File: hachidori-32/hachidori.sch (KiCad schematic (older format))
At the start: 55 parts, among them P1 VIN, P2 UART, P3 ADC, P4 I2C, SW1 FLASH, SW2 RESET, U1 NCP1117ST33, U2 MPU-9250, U3 ESP-13-WROOM-02, U4 BME280, U7 INA226

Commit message: Change esp chip
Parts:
- removed LED4, LED5: Front, droneworks:LED_1608mm, symbol LED-RESCUE-hachidori
- removed LED6, LED7: Back, droneworks:LED_1608mm, symbol LED-RESCUE-hachidori
- removed R28, R29, R30, R31: 220, rohm:MCR03, symbol R
- removed R3: 10k, rohm:MCR03, symbol R
- removed U3: ESP-13-WROOM-02, droneworks:ESP-WROOM-02, symbol ESP-13-WROOM-02
- removed U?: 74AUP1G19, symbol 74AUP1G19
- added U?: ESP-WROOM-32, symbol ESP-WROOM-32
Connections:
- net labels removed: CS_2MP
- wire segments 291 -> 171
- no-connect marks 6 -> 5
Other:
- moved on the sheet: CB10, CB11, CB5, CB6, P2, P3, P4, R10, R26, R27, R4, R5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

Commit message: fix connections
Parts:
- removed CB? (x3): 104, droneworks:GRM18, symbol C
- removed P3: ADC, droneworks:Pin_Header_1x03, symbol CONN_01X03
- removed P?: SWD, symbol CONN_01X04
- removed P? (x2): PIO, symbol CONN_01X04
- removed P?: PIO, droneworks:Pin_Header_1x03, symbol CONN_01X03
- removed R2, R5: 10k, rohm:MCR03, symbol R
- removed R6: 20k, rohm:MCR03, symbol R
- removed R8: 2k, rohm:MCR03, symbol R
- removed U?: LPC812M101JDH20, symbol LPC812M101JDH20
- added P?: PWM, droneworks:Pin_Header_1x04, symbol CONN_01X04
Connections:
- net labels added: CS1, U2RXD, U2TXD, VBUS, VIN+, VIN-, VSPI_CLK, VSPI_CS0, VSPI_MISO, VSPI_MOSI
- net labels removed: ESP-RXD, ESP-TXD, HSPI_CLK, HSPI_CS, HSPI_MISO, HSPI_MOSI, LPC_CS, MPU_CS, SWCLK, SWDIO, TOUT, TOUTpin
- wire segments 171 -> 179
- no-connect marks 5 -> 11
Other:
- note added: "MPU_SPI0_CS"
- note added: "MPU_SPI0_SCLK"
- note removed: "I2C_SCL"
- note removed: "I2C_SDA"
- note removed: "LPC_SPI0_SI"
- note removed: "LPC_SPI0_SLK"
- note removed: "LPC_SPI0_SO"
- note removed: "MPU_SPI0_SLK"
- moved on the sheet: CB1, CB10, CB11, CB2, CB3, CB4, CB5, CB6, CE1, CE2, LED1, P1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

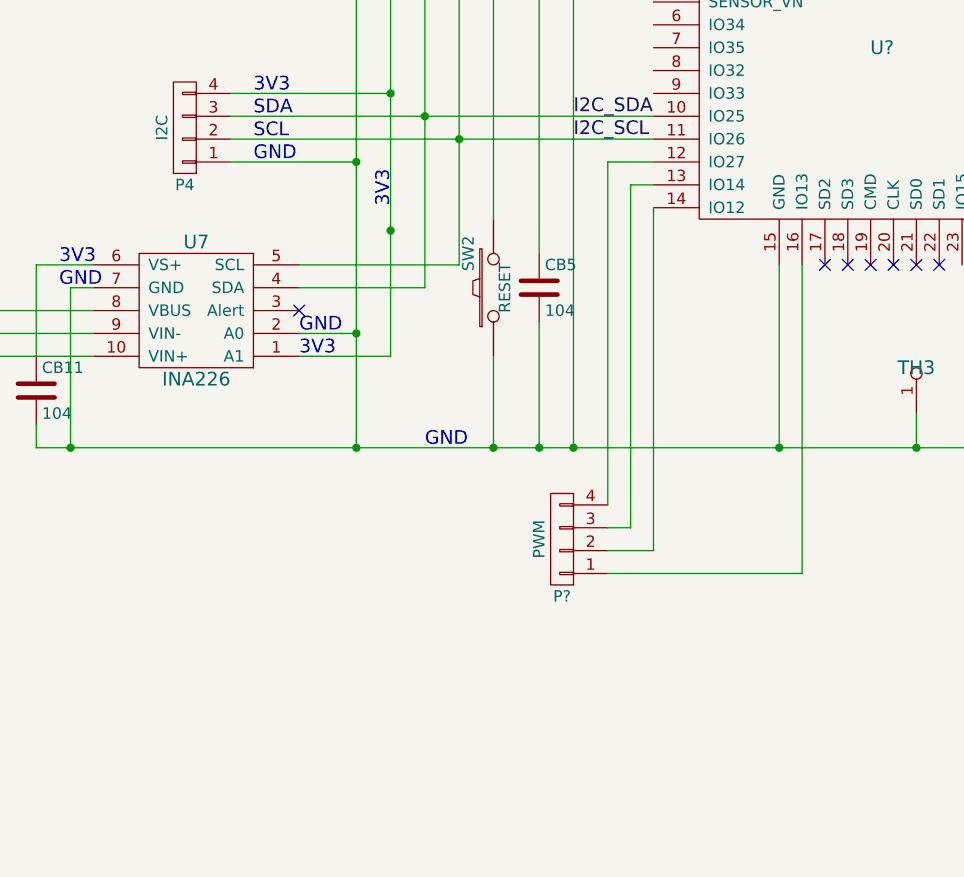
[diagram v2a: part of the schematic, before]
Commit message: Add ESC Interface
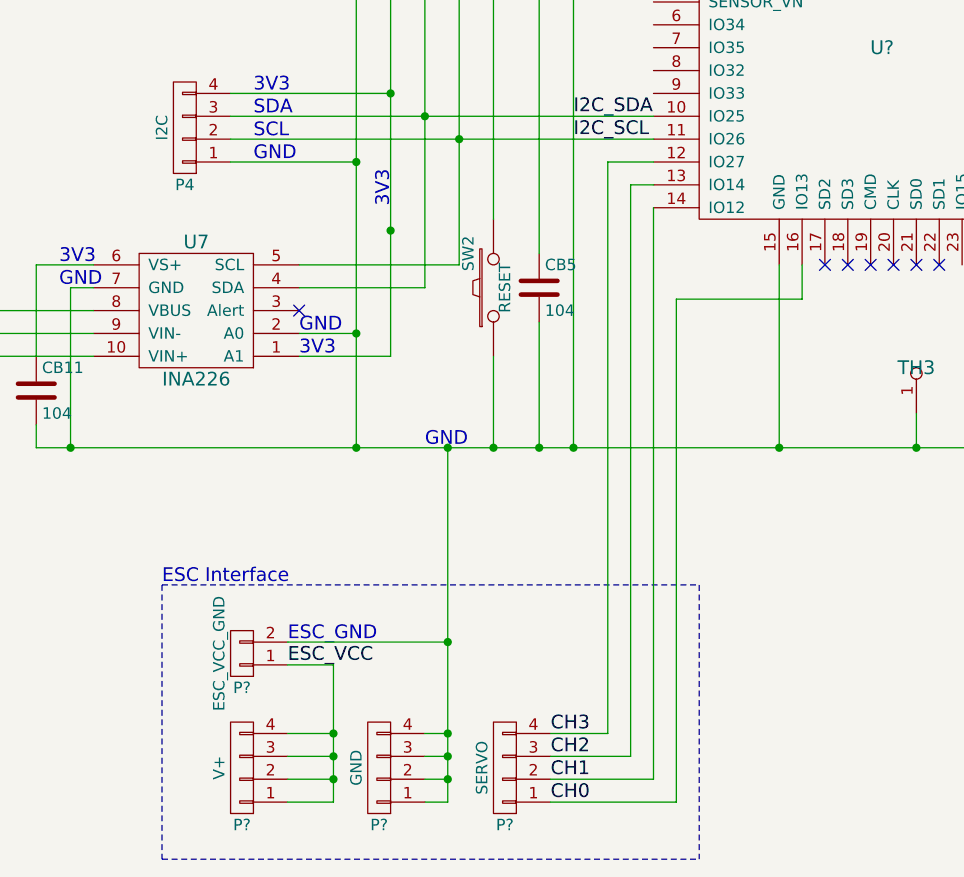
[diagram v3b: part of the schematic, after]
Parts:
- added P?: GND, droneworks:Pin_Header_1x04, symbol CONN_01X04
- added P?: V+, droneworks:Pin_Header_1x04, symbol CONN_01X04
- added P?: ESC_VCC_GND, droneworks:Pin_Header_1x02, symbol CONN_01X02
- P?: value PWM -> SERVO
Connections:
- net GND: now also P?.1 (P1), P?.2 (P2), P?.2 (P2), P?.3 (P3), P?.4 (P4)
- net CH3: now reaches P?.4 (P4), U?.12 (IO27)
- net CH2: now reaches P?.3 (P3), U?.13 (IO14)
- net CH1: now reaches P?.2 (P2), U?.14 (IO12)
- net CH0: now reaches P?.1 (P1), U?.16 (IO13)
- new net ESC_VCC: P?.1 (P1), P?.1 (P1), P?.2 (P2), P?.3 (P3), P?.4 (P4)
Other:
- note added: "ESC Interface"
- note added: "ESC_GND"
- moved on the sheet: P?

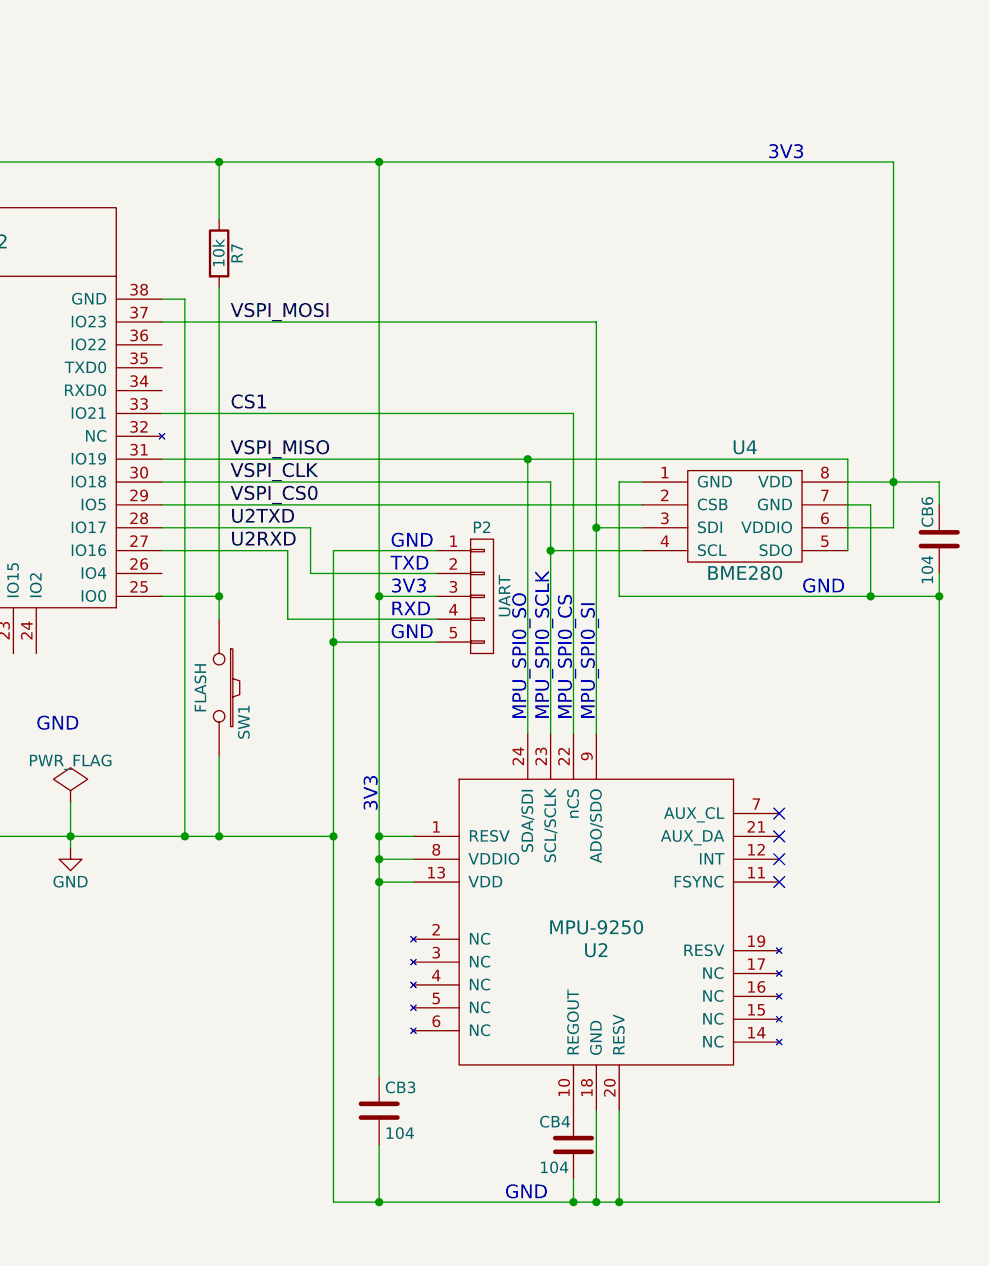
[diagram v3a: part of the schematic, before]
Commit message: Add UART Interface
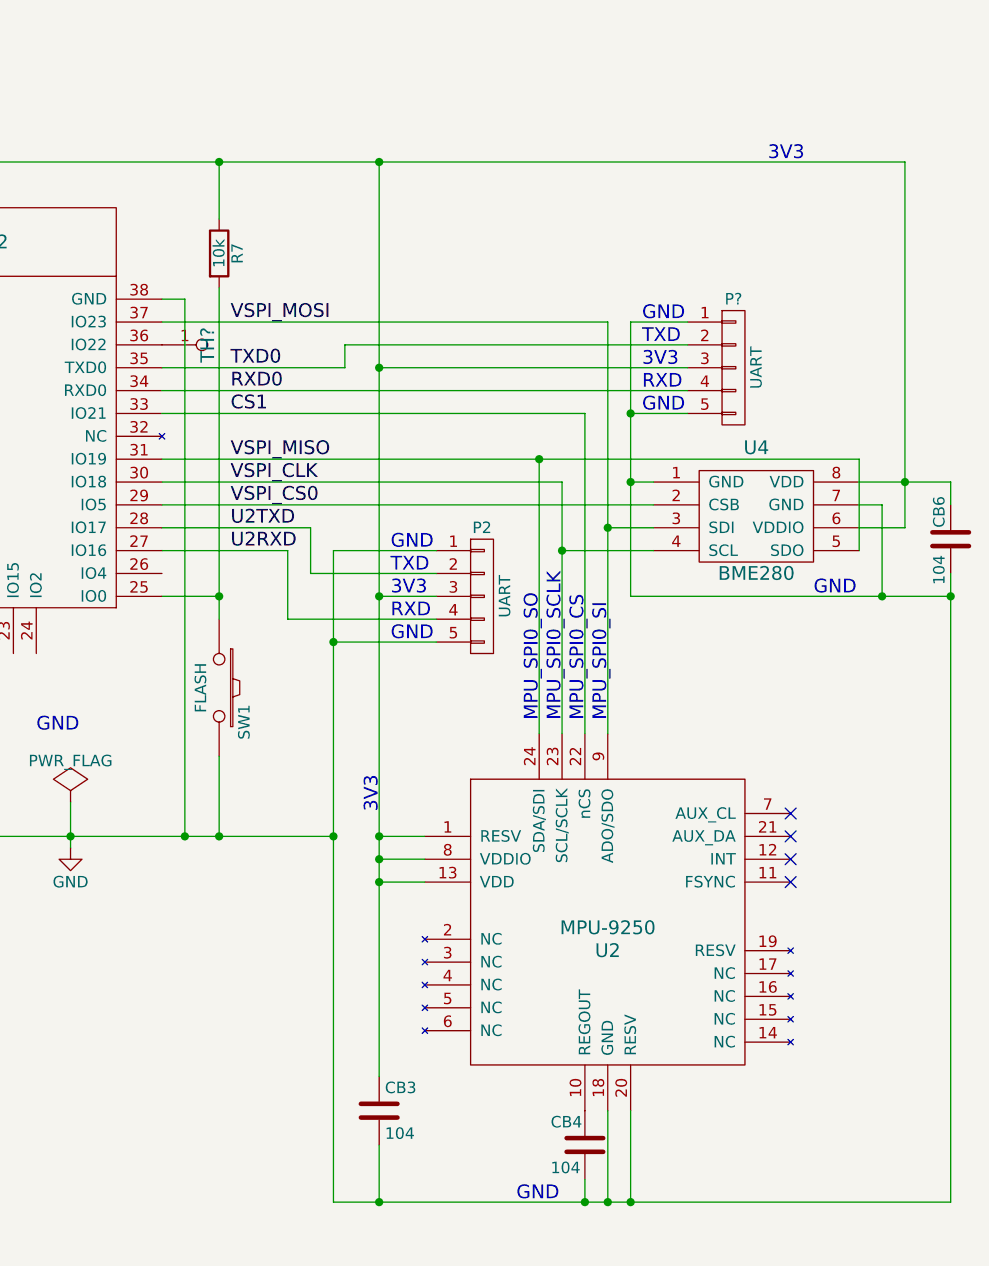
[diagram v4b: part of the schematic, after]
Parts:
- added P?: UART, droneworks:Pin_Header_1x05, symbol CONN_01X05
- added TH?: GND, droneworks:TH, symbol throughhole
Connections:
- net 3V3: now also P?.3 (P3)
- net GND: now also P?.1 (P1), P?.5 (P5)
- net RXD0: now reaches U?.34 (RXD0)
- net RXD0: now also P?.4 (P4)
- net TXD0: now reaches U?.35 (TXD0)
- net TXD0: now also P?.2 (P2)
- net at U?.36 (IO22): now also TH?.1
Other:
- moved on the sheet: CB4, CB6, U2, U4

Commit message: fix wire
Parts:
- P?: value UART -> Program
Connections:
- net FLASH: now reaches R7.2, SW1.1, U?.25 (IO0)
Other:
- moved on the sheet: P?, SW1, TH3

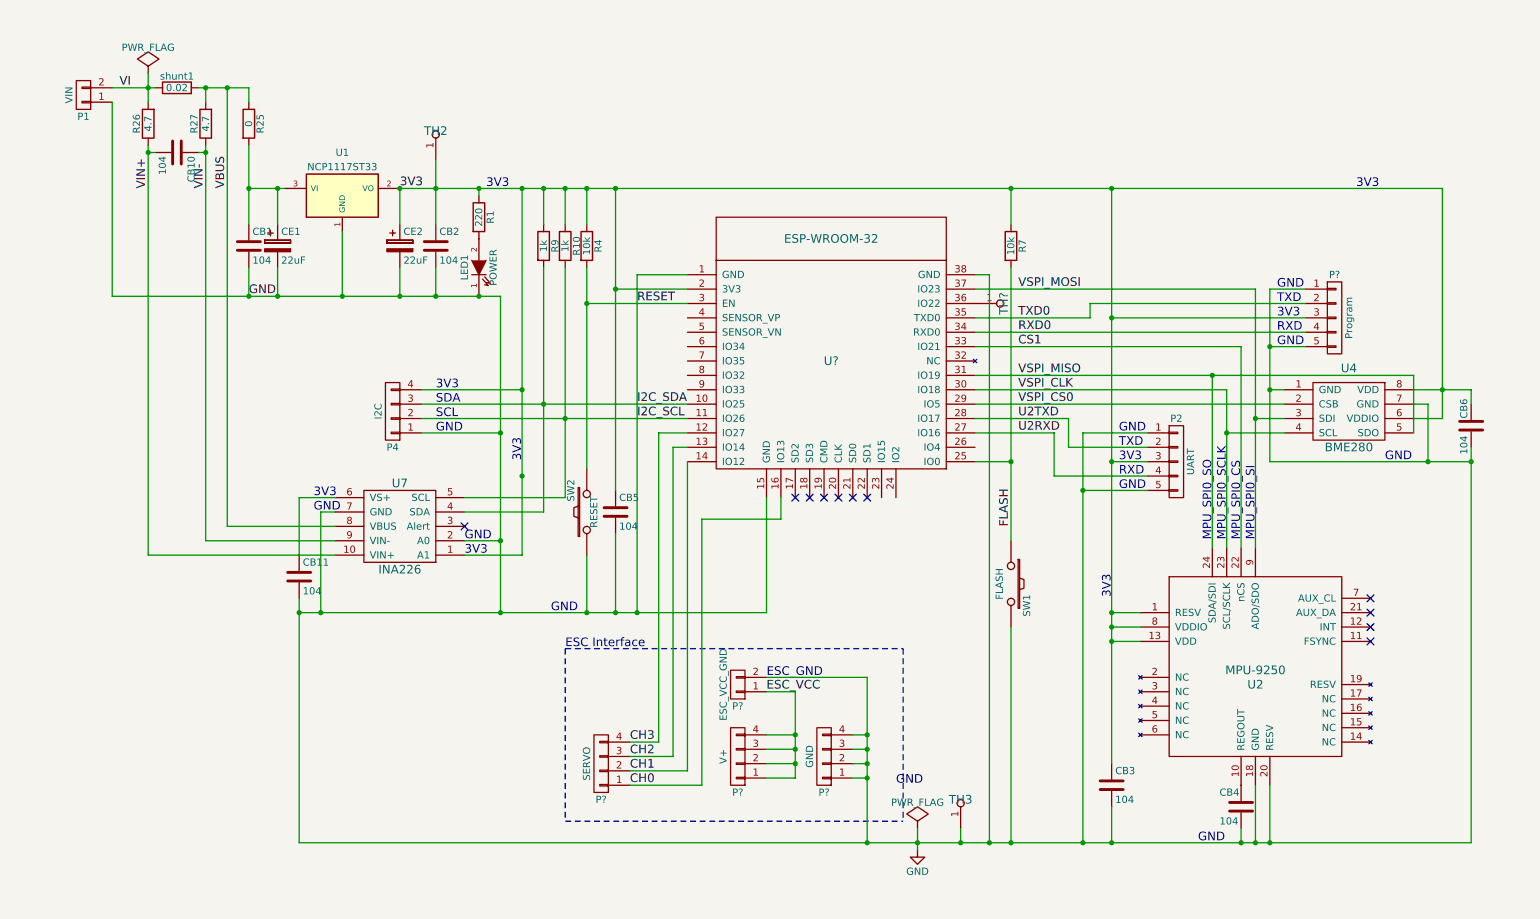
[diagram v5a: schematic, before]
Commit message: Add GPIO Interface
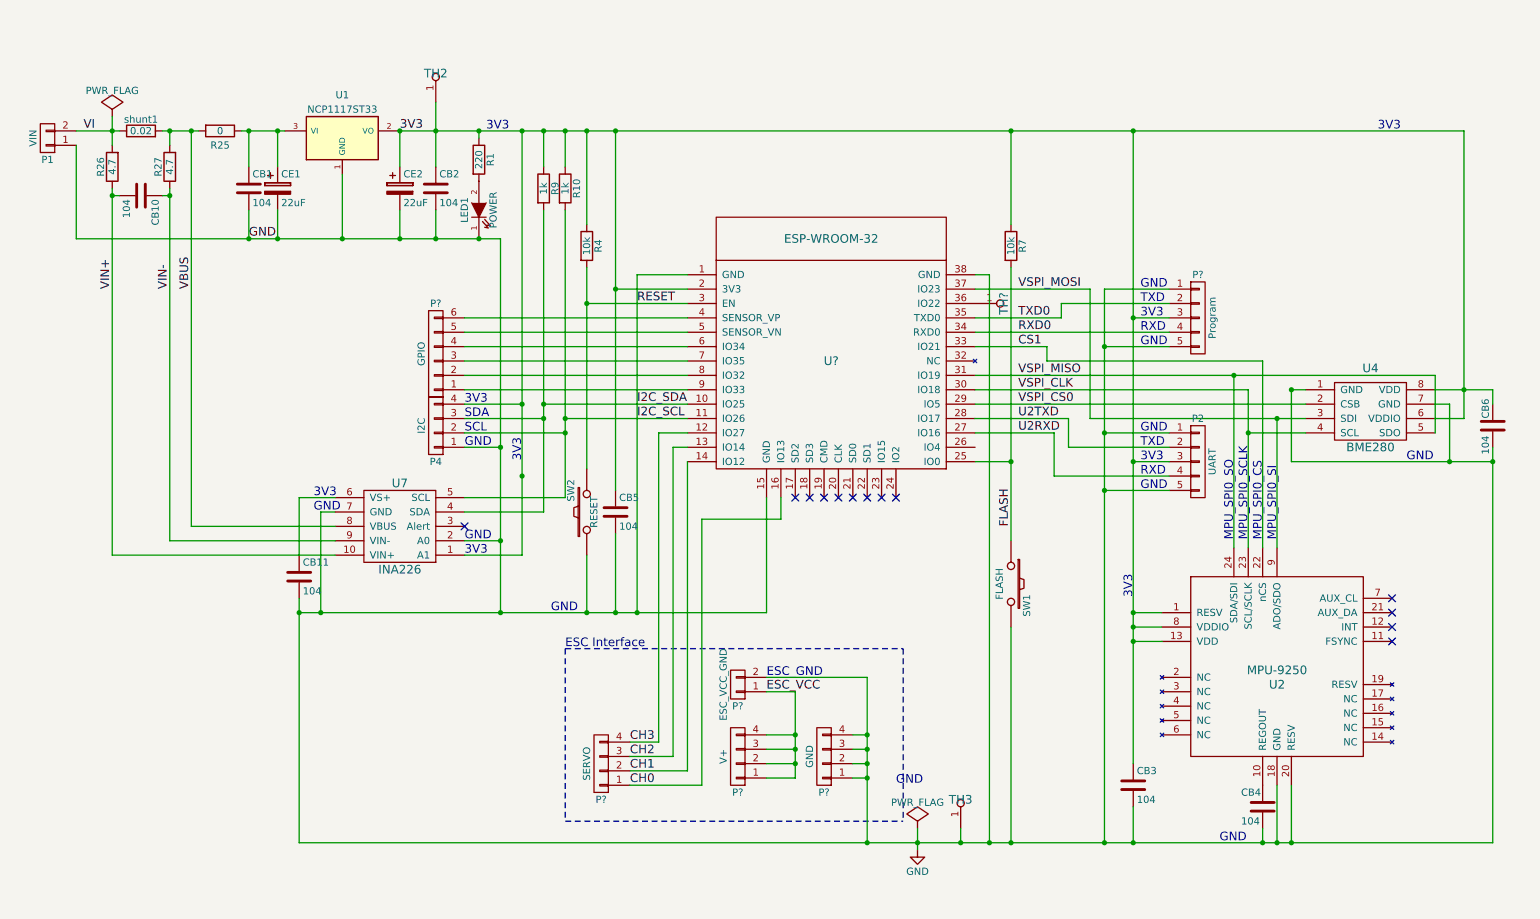
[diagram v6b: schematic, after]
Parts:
- added P?: GPIO, symbol CONN_01X06
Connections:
- net VBUS: now also R25.2; no longer R25.1
- net at CB1.1, CE1.1, U1.3 (VI): now also R25.1; no longer R25.2
- net at U?.4 (SENSOR_VP): now also P?.6 (P6)
- net at U?.5 (SENSOR_VN): now also P?.5 (P5)
- net at U?.6 (IO34): now also P?.4 (P4)
- net at U?.7 (IO35): now also P?.3 (P3)
- net at U?.8 (IO32): now also P?.2 (P2)
- net at U?.9 (IO33): now also P?.1 (P1)
- no-connect marks 11 -> 13
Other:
- moved on the sheet: CB1, CB10, CB2, CB3, CB4, CB6, CE1, CE2, LED1, P1, P2, P4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

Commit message: Connect GPIO35 to MPU_INT
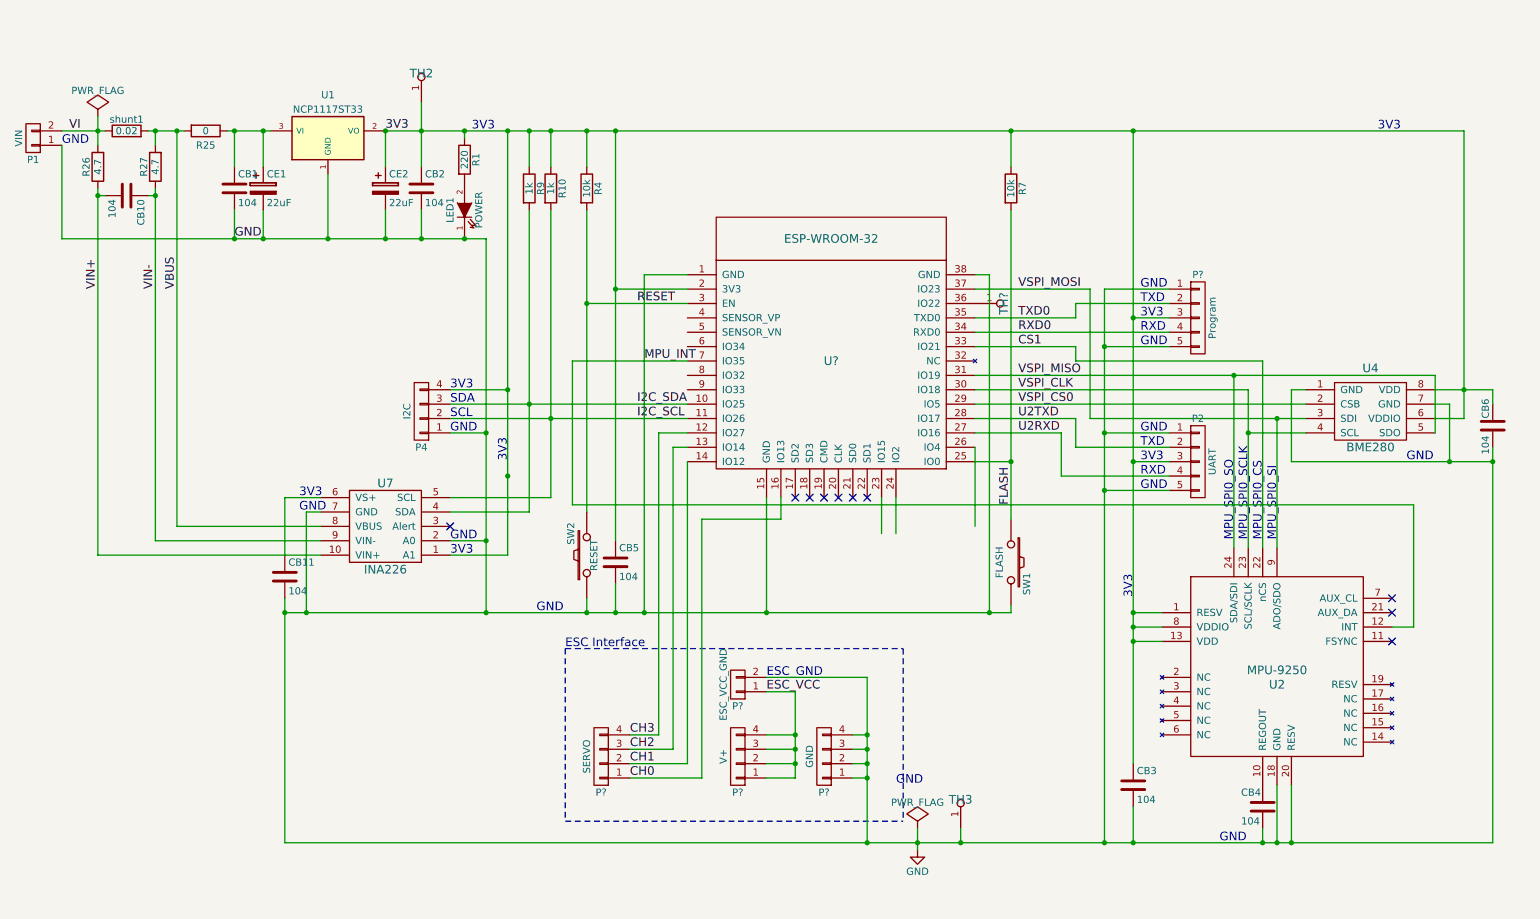
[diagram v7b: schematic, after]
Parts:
- removed P?: GPIO, symbol CONN_01X06
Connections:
- net FLASH is gone; now on net GND: R7.2, SW1.1, U?.25 (IO0)
- net GND: now also U2.12 (INT), U?.7 (IO35); no longer P4.2 (P2), P4.3 (P3), R10.2, R4.2, R9.2, SW2.2, U7.4 (SDA), U7.5 (SCL), U?.10 (IO25), U?.11 (IO26), U?.3 (EN)
- new net I2C_SCL: P4.2 (P2), R10.2, U7.5 (SCL), U?.11 (IO26)
- new net I2C_SDA: P4.3 (P3), R9.2, U7.4 (SDA), U?.10 (IO25)
- new net RESET: R4.2, SW2.2, U?.3 (EN)
- no-connect marks 13 -> 10
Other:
- moved on the sheet: CB1, CB10, CB11, CB2, CB5, CE1, CE2, LED1, P1, P4, P?, R1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
